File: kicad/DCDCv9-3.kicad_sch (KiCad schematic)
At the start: 198 parts, among them J1 43650-0315, J1.1 43645-0300, J1.2 Conn_01x01_Pin, J1.3 Conn_01x01_Pin, J1.4 Conn_01x01_Pin, J2 Conn_01x02_Male, J3 Conn_01x02, J3.1 Conn_01x02, J3.2 Conn_01x01_Pin, J3.3 Conn_01x01_Pin, J4 Conn_01x02_Male, J5 XT60 Male, J5.1 XT60 Female (wrong symbol ik), J6 Conn_01x02_Male, J7 Conn_01x02_Male, J8 Conn_01x02_Male, M1 Fan, Q1 PMV20ENR, Q10 IMBG65R050M2HXTMA1, Q11 IMBG65R050M2HXTMA1, Q2 PMV20ENR, Q3 SIHP24N80AE-GE3, Q4 IXYP8N90C3, Q5 PMV20ENR, Q6 PMV20ENR, Q7 PMV20ENR, T1 DIY Transformer ETD 39, T1.1 Ferrite Core, T1.2 Ferrite Core (gapped), T1.3 1800 mm 120 x 0.1 mm HF litz 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, T1.4 165 mm 600 x 0,071 mm HF litz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, T1.5 165 mm 600 x 0,071 mm HF litz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, U1 RP-1515S, U10 LM2904BIDDFR, U11 UCC21520DW, U12 UCC25600, U13 ZXRE330ASA-7, U14 LM2904BIDDFR, U2 RT9058-90GVL, U3 MP4541_SOP8-EP, U4 TLV61048DBVR, U6 LM2904BIDDFR, U7 TL431BCDBZR, U9 ACPL-217-50AE

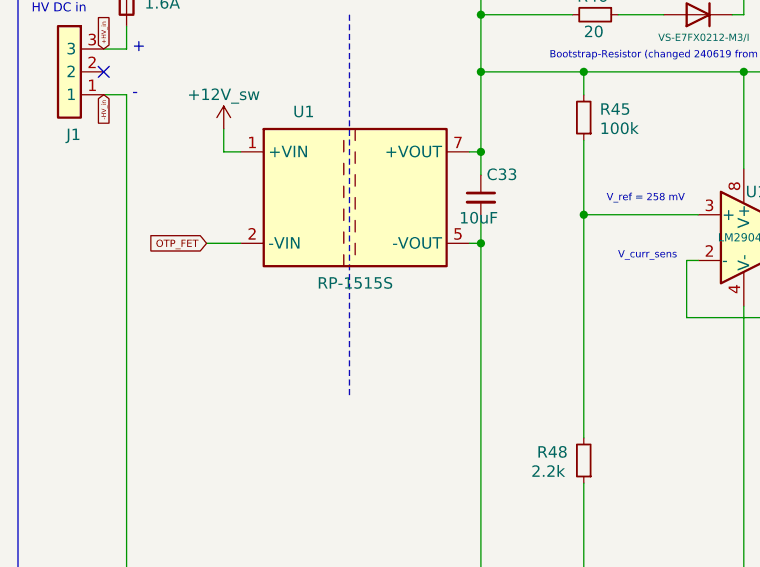
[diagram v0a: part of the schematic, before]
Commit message: Fixed U1 (see Build notes 260410), updated BOMs
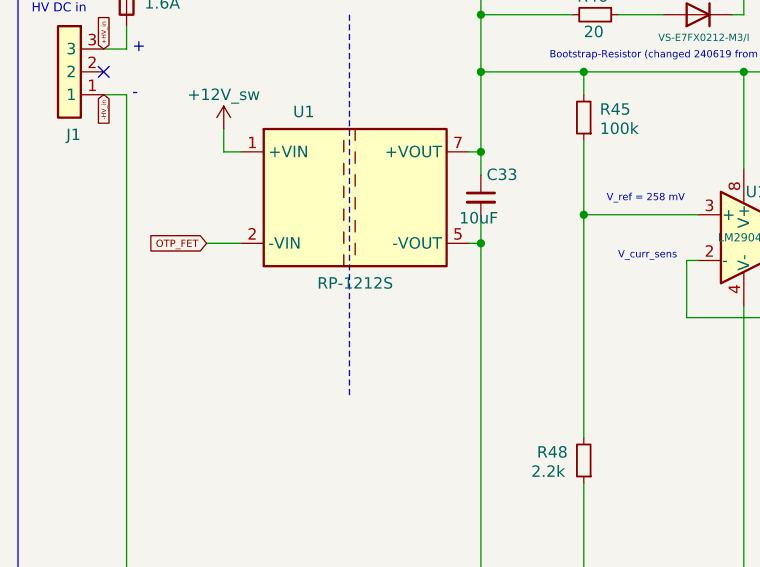
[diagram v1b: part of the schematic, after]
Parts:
- U1: value RP-1515S -> RP-1212S; Manufacturer_Part_Number RP-1515S -> RP-1212S
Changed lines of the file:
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@@
 	(title_block
 		(title "DC/DC v9-3r1.4")
-		(date "2026-03-14")
+		(date "2026-05-11")
 		(company "Author: Rootthecause")
 	)
@@
 			)
 		)
-		(property "Value" "RP-1515S"
+		(property "Value" "RP-1212S"
 			(at 50.8 62.865 0)
 			(effects
@@
 			)
 		)
-		(property "Datasheet" "https://www.mouser.de/ProductDetail/RECOM-Power/RP-1515S?qs=8OBu2JtKQqqZy6hEc5gvsA%3D%3D"
+		(property "Datasheet" "https://www.mouser.de/ProductDetail/RECOM-Power/RP-1212S?qs=YWgezujkI1KjTZkjNYMtQA%3D%3D"
 			(at 50.8 66.04 0)
 			(effects
@@
 			)
 		)
-		(property "Manufacturer_Part_Number" "RP-1515S"
+		(property "Manufacturer_Part_Number" "RP-1212S"
 			(at 50.8 53.34 0)
 			(effects

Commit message: added MP4581 as replacement for MP4541
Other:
- note added: "If the MP4541 is not available, use the MP4581 (1:1 compatible, 100V variant)"
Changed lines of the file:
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@@
+		)
+	)
+	(text "If the MP4541 is not available, \nuse the MP4581 (1:1 compatible, 100V variant)"
+		(exclude_from_sim no)
+		(at 41.275 224.79 0)
+		(effects
+			(font
+				(size 0.8 0.8)
+			)
+			(justify left bottom)
 		)
 	)
